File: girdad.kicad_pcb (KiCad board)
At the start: 2 copper layers, 20.5 x 35.5 mm, 21 parts, among them J1 USB_C_Plug_USB2.0, U1 CP2102N-Axx-xQFN28, U2 MCP2122-E/SN, U3 TFBS4711-TR1

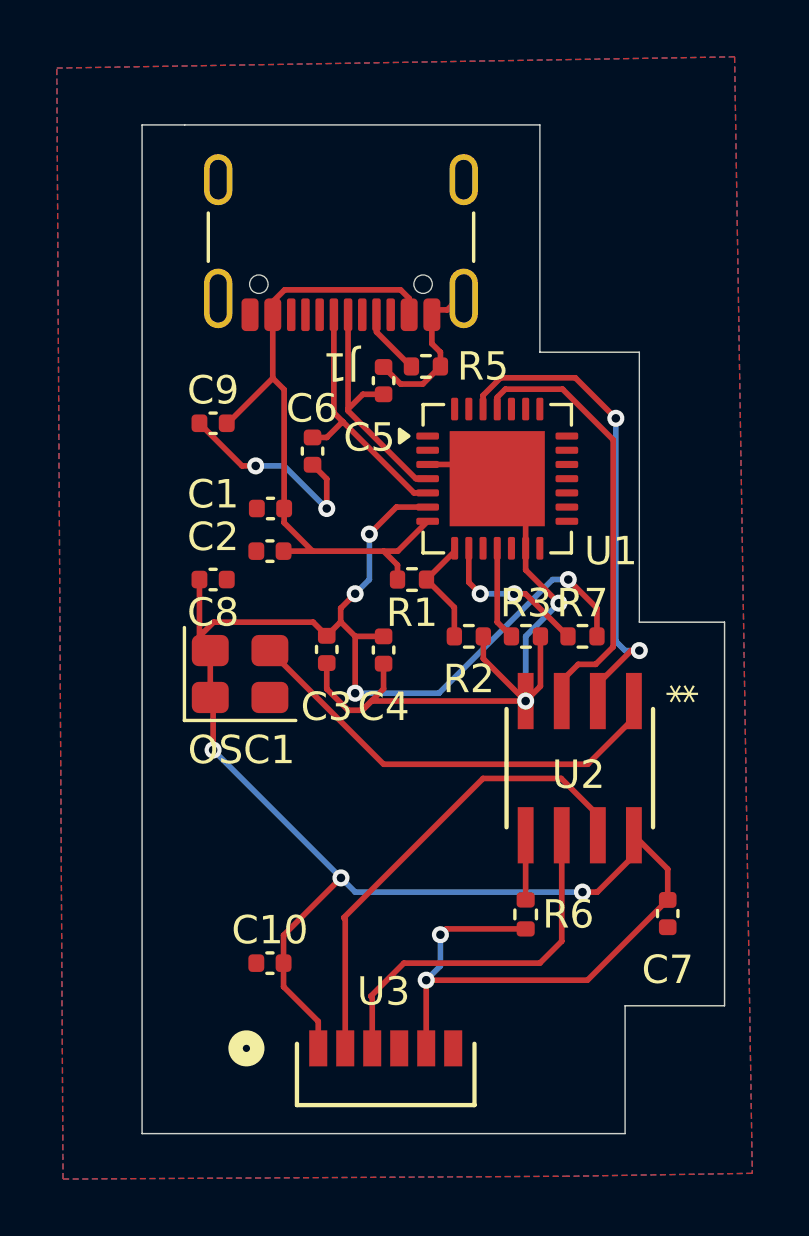
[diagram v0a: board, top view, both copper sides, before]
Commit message: Add mounting holes and silkscreen images and messages (More to come)
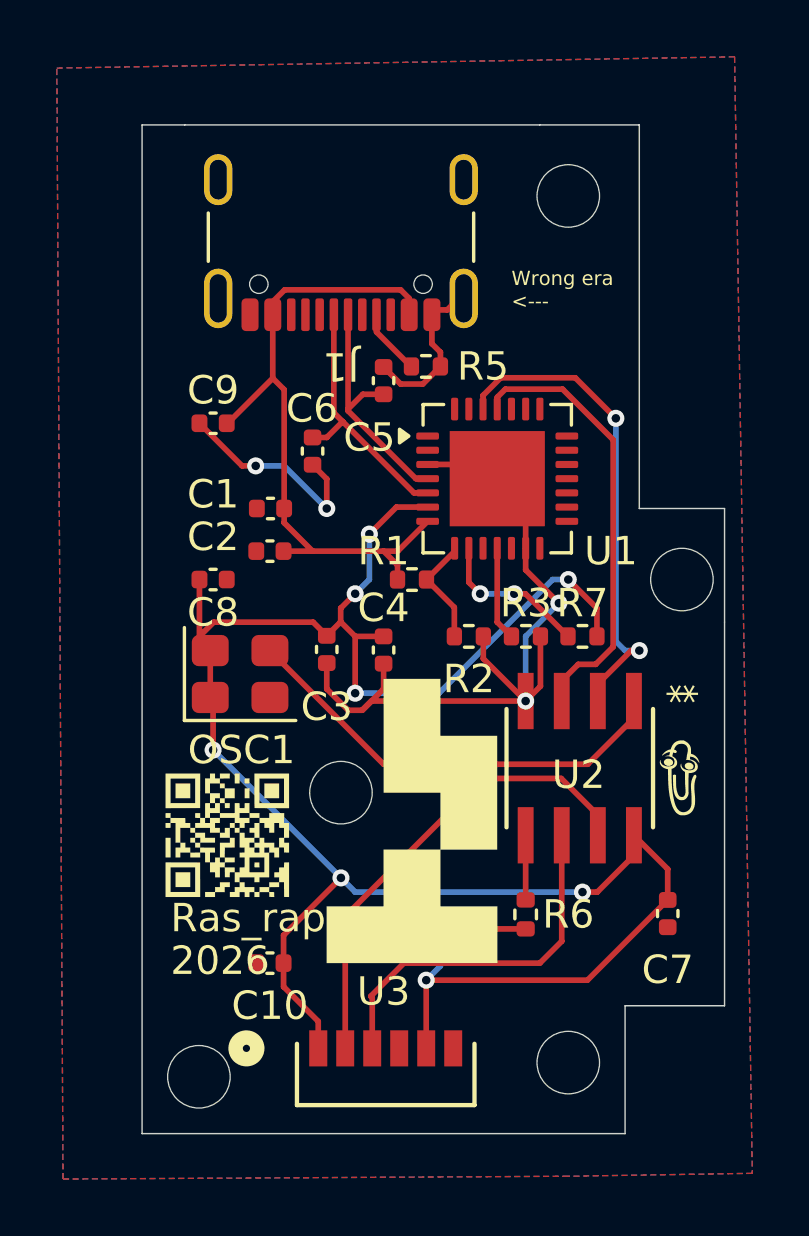
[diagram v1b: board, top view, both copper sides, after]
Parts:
- added G***: LOGO, LOGO, F.Cu at (48.0, 48.0)
- added G***: LOGO, LOGO, B.Cu at (40.0, 54.5)
- added G***: LOGO, LOGO, B.Cu at (56.5, 48.5)
- added G***: LOGO, LOGO, F.Cu at (56.5, 48.5)
- added G***: LOGO, LOGO, F.Cu at (47.0, 53.0)
- added G***: LOGO, LOGO, F.Cu at (40.5, 50.5)
- added G***: LOGO, LOGO, B.Cu at (45.0, 27.0)
- added G***: LOGO, LOGO, B.Cu at (46.0, 58.5)
- added G***: LOGO, LOGO, B.Cu at (54.0, 49.5)
- added G***: LOGO, LOGO, B.Cu at (45.6, 35.5)
- added G***: LOGO, LOGO, B.Cu at (50.5, 36.5)
- added REF**: MountingHole_2.2mm_M2, MountingHole:MountingHole_2.2mm_M2, F.Cu at (44.5, 49.0)
- added REF**: MountingHole_2.2mm_M2, MountingHole:MountingHole_2.2mm_M2, F.Cu at (52.5, 58.5)
- added REF**: MountingHole_2.2mm_M2, MountingHole:MountingHole_2.2mm_M2, F.Cu at (52.5, 28.0)
- added REF**: MountingHole_2.2mm_M2, MountingHole:MountingHole_2.2mm_M2, F.Cu at (56.5, 41.5)
- added REF**: MountingHole_2.2mm_M2, MountingHole:MountingHole_2.2mm_M2, F.Cu at (39.5, 59.0)
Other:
- outline, holes or cut-outs redrawn
- board text added: "*may need drivers"
- board text added: "2026"
- board text added: "GIrDAd Great Infrared Data Assosiation Dongle"
- board text added: "Looks like you're using IrDA."
- board text added: "Ras_rap"
- board text added: "What bluetooth wanted to be"
- board text added: "Why?"
- board text added: "Wrong era <---"
- board text added: "if found i probably dropped it under my desk"
- board text added: "no drivers needed*"

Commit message: Enough silkscreen
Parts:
- added G***: LOGO, LOGO, B.Cu at (44.0, 51.0)
- moved G*** 20.6 mm to (40.5, 34.0)
- moved G*** 17.0 mm to (55.0, 46.5)
- moved G*** 13.1 mm to (46.7, 39.7)
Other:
- board text added: "*insert more references here*"
